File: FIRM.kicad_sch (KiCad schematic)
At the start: 98 parts, among them J1 Conn_01x02_Pin, J2 DM3CS-SF, Q2 IRLML6402, SW1 PTS815, U1 STM32F405RGTx, U2 MIC5219-3.3YM5, U6 A-USBC-20F0-EA-GSR05, U7 W25Q128JVS, X2 32.768khz, Y1 12 MHz

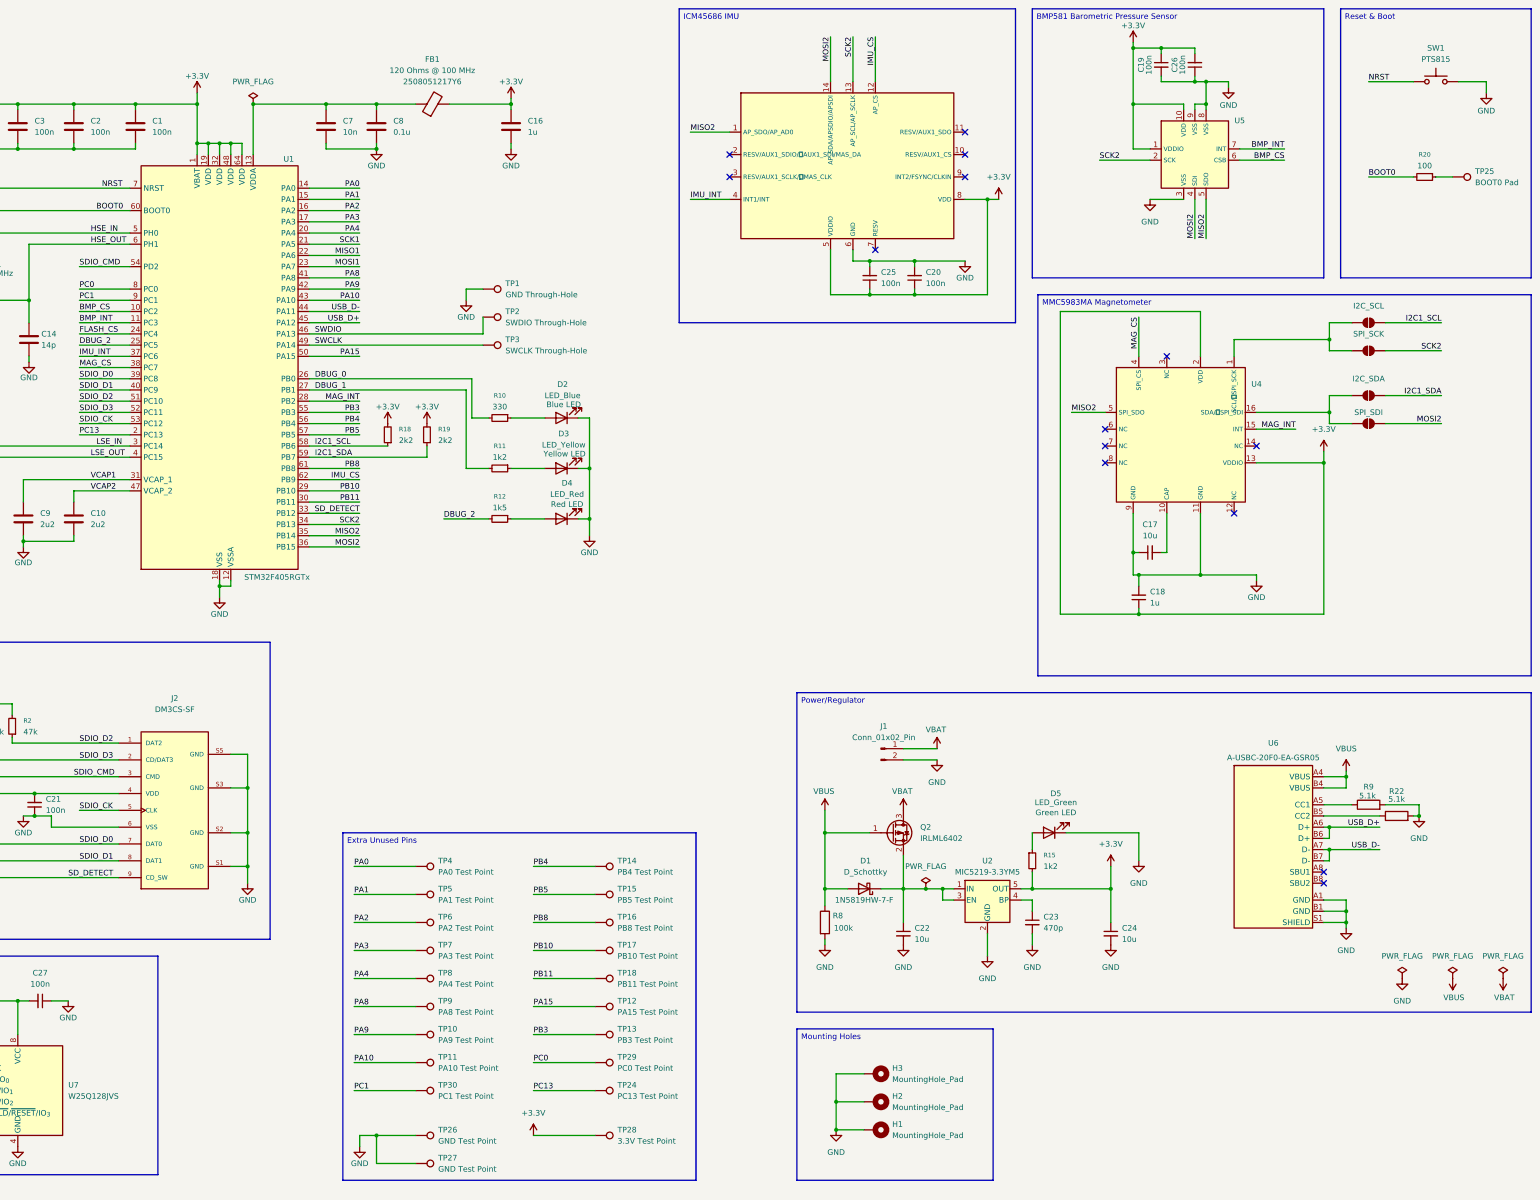
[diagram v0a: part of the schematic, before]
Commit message: winter schematic changes
added high-g accelerometer, changed magnetometer to spi only, changed debug pins, added spi/i2c test pads, added INT/CS test pads, and replaced NRST button with test pad.
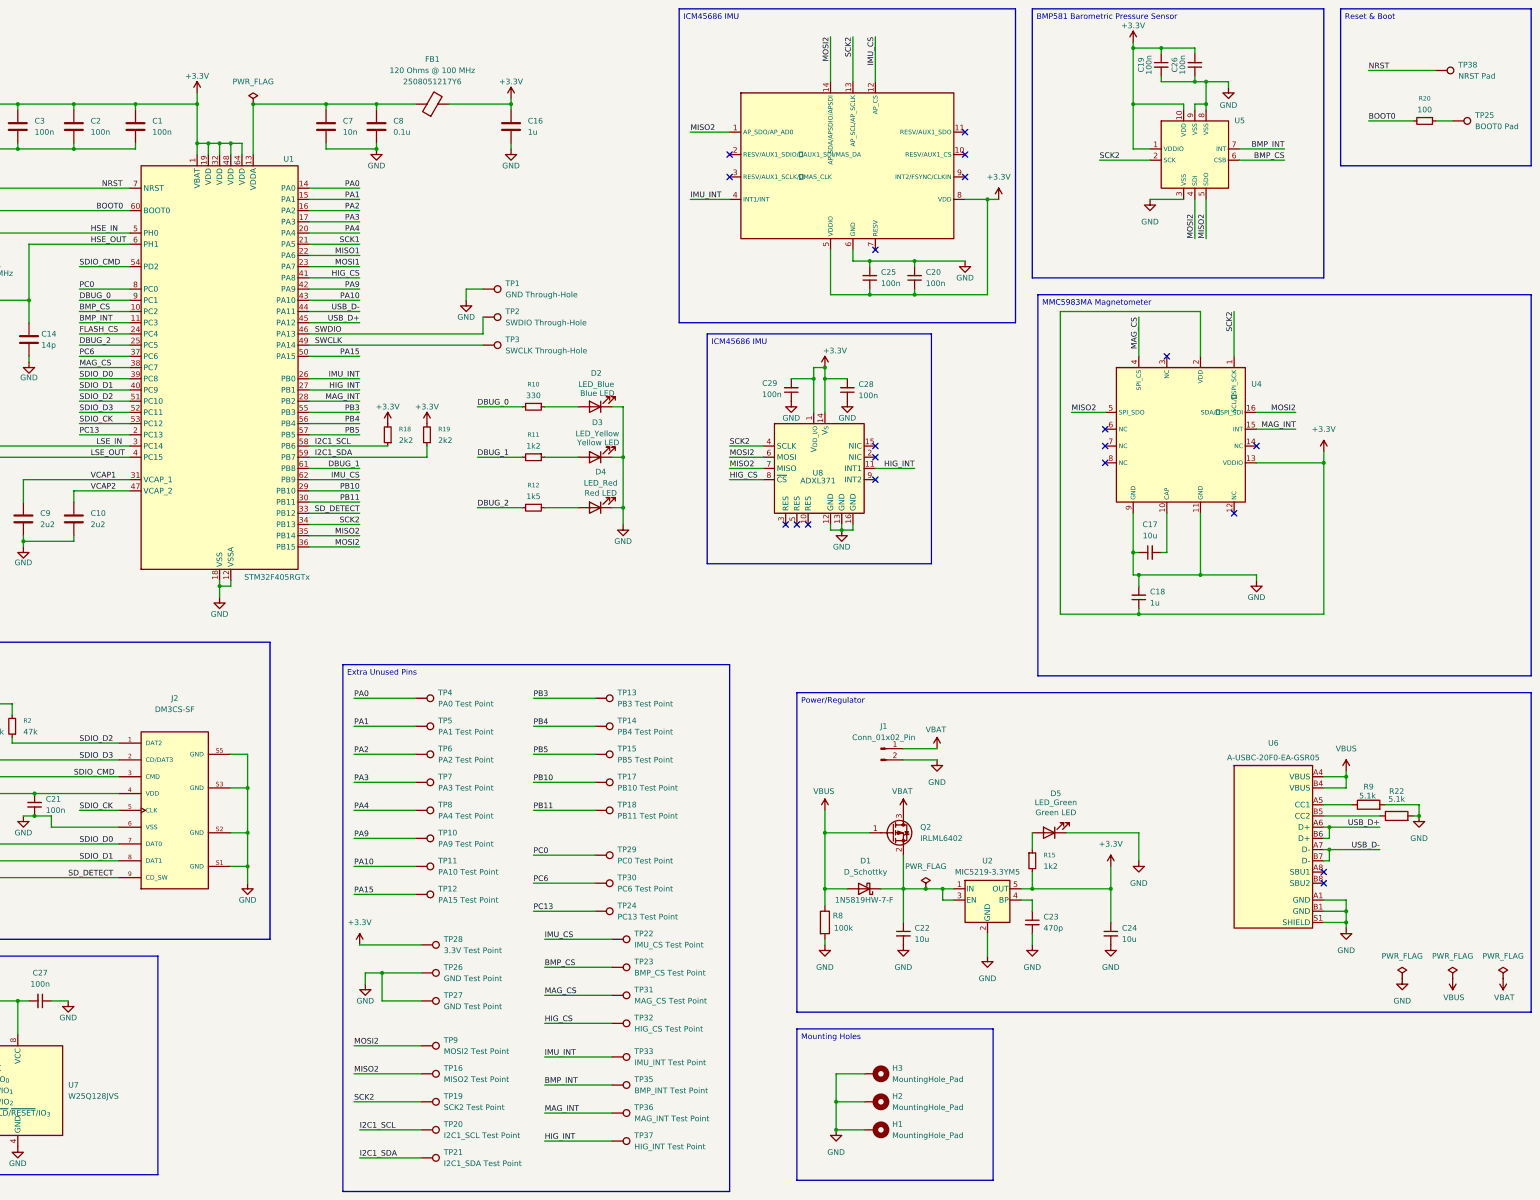
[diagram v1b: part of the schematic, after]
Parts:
- removed JP1: I2C_SDA, Jumper:SolderJumper-2_P1.3mm_Open_RoundedPad1.0x1.5mm, symbol Jumper:SolderJumper_2_Open
- removed JP2: SPI_SDI, Jumper:SolderJumper-2_P1.3mm_Open_RoundedPad1.0x1.5mm, symbol Jumper:SolderJumper_2_Open
- removed JP3: I2C_SCL, Jumper:SolderJumper-2_P1.3mm_Open_RoundedPad1.0x1.5mm, symbol Jumper:SolderJumper_2_Open
- removed JP4: SPI_SCK, Jumper:SolderJumper-2_P1.3mm_Open_RoundedPad1.0x1.5mm, symbol Jumper:SolderJumper_2_Open
- removed SW1: PTS815, Button_Switch_SMD:SW_SPST_PTS810, symbol Switch:SW_Push
- added C28, C29: 100n, Capacitor_SMD:C_0603_1608Metric, symbol Device:C_Small
- added TP19: SCK2 Test Point, TestPoint:TestPoint_Pad_1.0x1.0mm, symbol Connector:TestPoint
- added TP20: I2C1_SCL Test Point, TestPoint:TestPoint_Pad_1.0x1.0mm, symbol Connector:TestPoint
- added TP21: I2C1_SDA Test Point, TestPoint:TestPoint_Pad_1.0x1.0mm, symbol Connector:TestPoint
- added TP22: IMU_CS Test Point, TestPoint:TestPoint_Pad_1.0x1.0mm, symbol Connector:TestPoint
- added TP23: BMP_CS Test Point, TestPoint:TestPoint_Pad_1.0x1.0mm, symbol Connector:TestPoint
- added TP31: MAG_CS Test Point, TestPoint:TestPoint_Pad_1.0x1.0mm, symbol Connector:TestPoint
- added TP32: HIG_CS Test Point, TestPoint:TestPoint_Pad_1.0x1.0mm, symbol Connector:TestPoint
- added TP33: IMU_INT Test Point, TestPoint:TestPoint_Pad_1.0x1.0mm, symbol Connector:TestPoint
- added TP35: BMP_INT Test Point, TestPoint:TestPoint_Pad_1.0x1.0mm, symbol Connector:TestPoint
- added TP36: MAG_INT Test Point, TestPoint:TestPoint_Pad_1.0x1.0mm, symbol Connector:TestPoint
- added TP37: HIG_INT Test Point, TestPoint:TestPoint_Pad_1.0x1.0mm, symbol Connector:TestPoint
- added TP38: NRST Pad, TestPoint:TestPoint_Pad_1.0x1.0mm, symbol Connector:TestPoint
- added U8: ADXL371, Sensor_Motion:Analog_LGA-16_3.25x3mm_P0.5mm_LayoutBorder3x5y, symbol Sensor_Motion:ADXL363
- TP10, TP11, TP12, TP13, TP14, TP15, TP17, TP18, TP24, TP26, TP27, TP28, TP29, TP4, TP5, TP6, TP7: footprint TestPoint:TestPoint_THTPad_1.5x1.5mm_Drill0.7mm -> connectors:Testpoint_1.5x1.5mm_1.0mm
- TP16: value PB8 Test Point -> MISO2 Test Point; footprint TestPoint:TestPoint_THTPad_1.5x1.5mm_Drill0.7mm -> TestPoint:TestPoint_Pad_1.0x1.0mm
- TP25: footprint TestPoint:TestPoint_Pad_1.5x1.5mm -> TestPoint:TestPoint_Pad_1.0x1.0mm
- TP30: value PC1 Test Point -> PC6 Test Point; footprint TestPoint:TestPoint_THTPad_1.5x1.5mm_Drill0.7mm -> connectors:Testpoint_1.5x1.5mm_1.0mm
- TP8: footprint TestPoint:TestPoint_THTPad_1.5x1.5mm_Drill0.7mm -> TestPoint:TestPoint_Pad_1.0x1.0mm
- TP9: value PA8 Test Point -> MOSI2 Test Point; footprint TestPoint:TestPoint_THTPad_1.5x1.5mm_Drill0.7mm -> TestPoint:TestPoint_Pad_1.0x1.0mm
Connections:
- net +3.3V: now also C28.2, C29.2, U8.1 (V_{DD_I/O}), U8.14 (V_{S})
- net BMP_CS: now also TP23.1
- net BMP_INT: now also TP35.1
- net DBUG_0: now also U1.9 (PC1); no longer U1.26 (PB0)
- net DBUG_1: now also U1.61 (PB8); no longer U1.27 (PB1)
- net GND: now also C28.1, C29.1, U8.12 (GND), U8.13 (GND), U8.16 (GND)
- net I2C1_SCL: now also TP20.1
- net I2C1_SDA: now also TP21.1
- net IMU_CS: now also TP22.1
- net IMU_INT: now also U1.26 (PB0), TP33.1; no longer U1.37 (PC6)
- net MAG_CS: now also TP31.1
- net MAG_INT: now also TP36.1
- net MISO2: now also TP16.1, U8.7 (MISO)
- net MOSI2: now also TP9.1, U4.16 (SDA/ SPI_SDI), U8.6 (MOSI)
- net NRST: now also TP38.1
- net SCK2: now also U4.1 (SCL/ SPI_SCK), TP19.1, U8.4 (SCLK)
- net PA8 renamed HIG_CS
- net HIG_CS: now also TP32.1, U8.8 (~{CS}); no longer TP9.1
- removed net PB8: TP16.1, U1.61 (PB8)
- net PC1 renamed PC6
- net PC6: now also U1.37 (PC6); no longer U1.9 (PC1)
- new net: U8.10 (RES), U8.13 (GND), U8.16 (GND)
- new net HIG_INT: TP37.1, U1.27 (PB1), U8.11 (INT1)
- no-connect marks 14 -> 20
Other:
- moved on the sheet: D2, D3, D4, R10, R11, R12, R20, TP10, TP11, TP12, TP13, TP14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

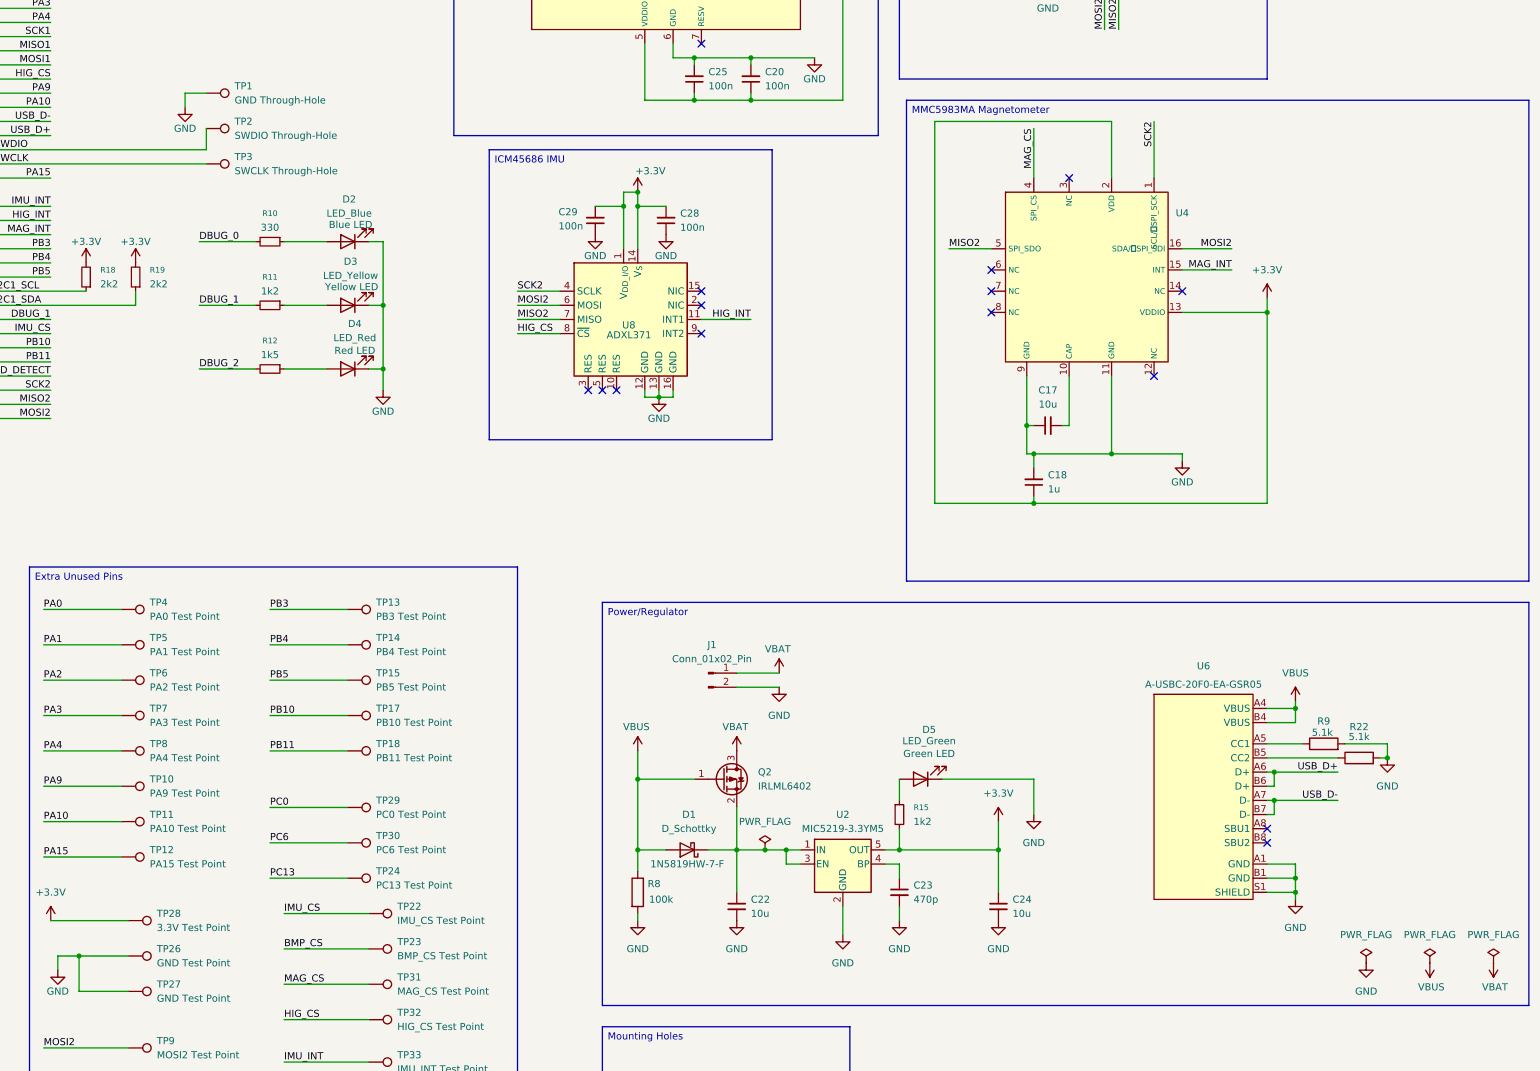
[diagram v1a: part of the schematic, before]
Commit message: Added voltage sensor
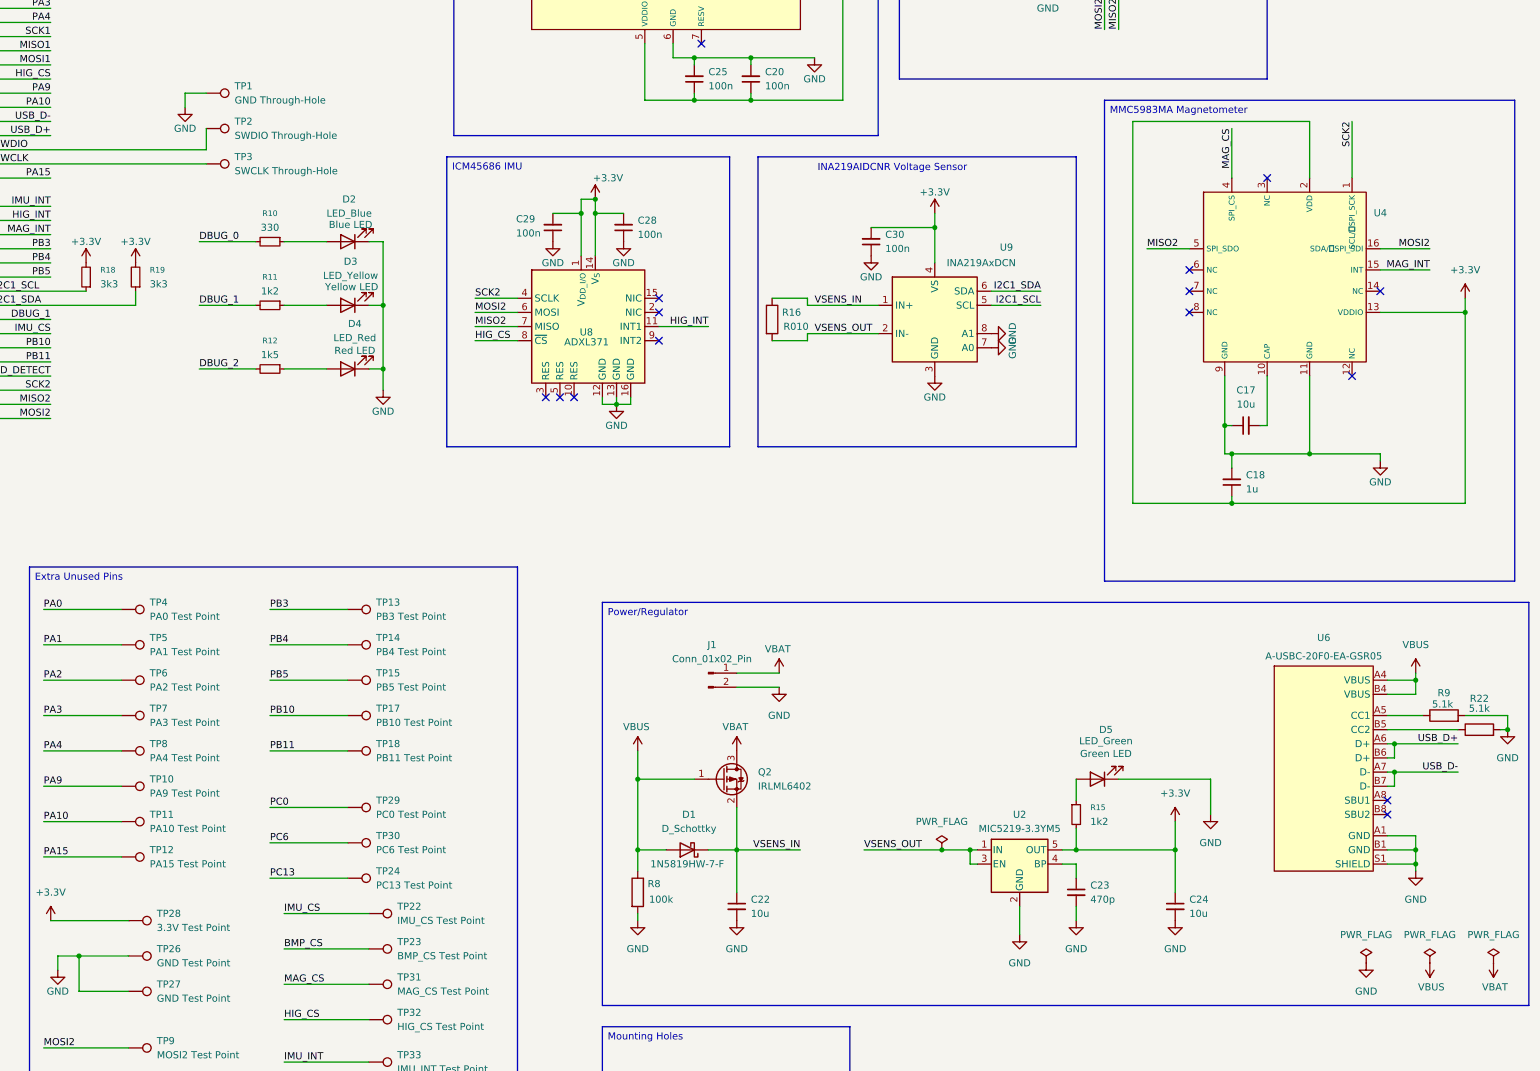
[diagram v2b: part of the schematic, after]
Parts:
- added C30: 100n, Capacitor_SMD:C_0603_1608Metric, symbol Device:C_Small
- added R16: R010, symbol Device:R
- added U9: INA219AxDCN, Package_TO_SOT_SMD:SOT-23-8, symbol Sensor_Energy:INA219AxDCN
- R18, R19: value 2k2 -> 3k3
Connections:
- net +3.3V: now also C30.2, U9.4 (VS)
- net GND: now also C30.1, U9.3 (GND), U9.7 (A0), U9.8 (A1)
- net I2C1_SCL: now also U9.5 (SCL)
- net I2C1_SDA: now also U9.6 (SDA)
- net VSENS_IN: now reaches C22.1, D1.1 (K), Q2.2 (S)
- net VSENS_IN: now also R16.1, U9.1 (IN+); no longer U2.1 (IN), U2.3 (EN)
- new net: U8.10 (RES), U8.13 (GND), U8.16 (GND)
- new net VSENS_OUT: R16.2, U2.1 (IN), U2.3 (EN), U9.2 (IN-)
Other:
- note added: "INA219AIDCNR Voltage Sensor"
- company: Seth O, Will S, Harshil M -> Seth O, Will S, Harshil M, Jackson E
- moved on the sheet: C17, C18, C23, C24, C28, C29, D5, R15, R22, R9, U2, U4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
